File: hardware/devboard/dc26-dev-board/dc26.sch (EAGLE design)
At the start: 105 parts, among them CN1 JST, IC3 LDL112D33R, J1 DC26 Shitty AddOn, J2 DC26 Shitty AddOn, M10 STM32-Breakout-2, P1 SSSS811101, Y1 ABL-8.000MHZ-B2

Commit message: dc26-'final' board ready
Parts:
- removed M10: STM32-Breakout-2, dc-26:M10SILK_FEMALE_PTH
- renumbered CHARGING_CIRCUT to CHARGE
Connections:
- net BUTTON_DOWN: no longer M10.8
- net BUTTON_FIRE1: no longer STM32-BREAKOUT.7
- net BUTTON_LEFT: no longer STM32-BREAKOUT.17
- net BUTTON_RIGHT: no longer STM32-BREAKOUT.5
- net BUTTON_UP: no longer M10.7
- net ESP-IO0: no longer ESP-BREAKOUT.25
- net ESP-RX0: no longer ESP-BREAKOUT.34
- net ESP-TX0: no longer ESP-BREAKOUT.35
- net ESP_I2C_SCL: now also ESP-BREAKOUT.9, STM32-BREAKOUT.5; no longer ESP-BREAKOUT.31, M10.5
- net ESP_I2C_SDA: now also ESP-BREAKOUT.8, STM32-BREAKOUT.3; no longer ESP-BREAKOUT.30, M10.6
- net ESP_INTER: now also STM32-BREAKOUT.8; no longer ESP-BREAKOUT.33, M10.1
- net ESP_RX_PIN_5: no longer ESP-BREAKOUT.29
- net ESP_TX_PIN_4: no longer ESP-BREAKOUT.26
- net GND: now also ESP-BREAKOUT.40; no longer ESP-BREAKOUT.38, M10.9
- net GPIO_APA102_DATA: no longer STM32-BREAKOUT.20
- net GPIO_APA106_DATA: no longer STM32-BREAKOUT.22
- net IO12: now also ESP-BREAKOUT.12; no longer ESP-BREAKOUT.14
- net IO13: now also ESP-BREAKOUT.14; no longer ESP-BREAKOUT.16
- net IO17: now also ESP-BREAKOUT.10; no longer ESP-BREAKOUT.28
- net IO22: now also ESP-BREAKOUT.4; no longer ESP-BREAKOUT.36
- net IO23: now also ESP-BREAKOUT.3; no longer ESP-BREAKOUT.37
- net IO25: now also ESP-BREAKOUT.26; no longer ESP-BREAKOUT.10
- net IO26: now also ESP-BREAKOUT.29; no longer ESP-BREAKOUT.11
- net IO27: now also ESP-BREAKOUT.28; no longer ESP-BREAKOUT.12
- net IO32: now also ESP-BREAKOUT.30; no longer ESP-BREAKOUT.8
- net IO33: now also ESP-BREAKOUT.31; no longer ESP-BREAKOUT.9
- net IO34: now also ESP-BREAKOUT.34; no longer ESP-BREAKOUT.6
- net IO35: now also ESP-BREAKOUT.33; no longer ESP-BREAKOUT.7
- net LCD_BACKLIGHT: no longer STM32-BREAKOUT.34
- net LCD_CS: no longer STM32-BREAKOUT.15
- net LCD_DATA_CMD: no longer STM32-BREAKOUT.13
- net LCD_RESET: no longer STM32-BREAKOUT.40
- net MID_BUTTON: no longer STM32-BREAKOUT.3
- net PA1: now also STM32-BREAKOUT.12; no longer STM32-BREAKOUT.25
- net PA7: now also STM32-BREAKOUT.13; no longer STM32-BREAKOUT.37
- net PB0: now also STM32-BREAKOUT.21; no longer STM32-BREAKOUT.38
- net PB1: now also STM32-BREAKOUT.37; no longer STM32-BREAKOUT.36
- net PB13: now also STM32-BREAKOUT.38; no longer STM32-BREAKOUT.21
- net PB15: now also STM32-BREAKOUT.36; no longer STM32-BREAKOUT.26
- net PB3: now also STM32-BREAKOUT.9; no longer M10.2
- net PB5: now also STM32-BREAKOUT.7; no longer M10.4
- net SENSOR_VN: now also ESP-BREAKOUT.11; no longer ESP-BREAKOUT.5
- net SENSOR_VP: now also ESP-BREAKOUT.16; no longer ESP-BREAKOUT.4
- net SPI2_LCD_MOSI: no longer STM32-BREAKOUT.19
- net SPI2_LCD_SCK: no longer STM32-BREAKOUT.32
- net SPI3_SD_SCK: now also STM32-BREAKOUT.40; no longer STM32-BREAKOUT.30
- net TIM_APA102_CLK: no longer STM32-BREAKOUT.18
- net USART1_RX_TO_ESP_TX_PIN_4: no longer STM32-BREAKOUT.12
- net USART1_TX_TO_ESP_RX_PIN_5: no longer STM32-BREAKOUT.14
- net VCC: no longer M10.10
- net VCC1: now also ESP-BREAKOUT.38
- net VIN: now also ESP-BREAKOUT.39

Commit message: logo causing 0 width polys will fix later
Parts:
- removed U$1: KRUX_LOGO, dc-26:KRUX_LOGO
- removed U$2: CMD_C0DE_LOGO, dc-26:CMD_C0DE_LOGO
- removed U$3: DARKNET_DD, dc-26:DARKNET_DD
- removed U$4: DARKNET_NN, dc-26:DARKNET_NN
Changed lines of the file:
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@@
 <part name="R9" library="dc-26" deviceset="RESISTOR" device="0805-RES" value="1M"/>
 <part name="GND70" library="dc-26" deviceset="GND" device=""/>
-<part name="U$3" library="dc-26" deviceset="DARKNET_D" device="D"/>
-<part name="U$4" library="dc-26" deviceset="DARKNET_N" device="N"/>
 <part name="D1" library="dc-26" deviceset="DIODE" device="SOD" value="1N4148WS"/>
 <part name="102-1" library="dc-26" deviceset="APA102" device="5050"/>
@@
 <part name="J2" library="dc-26" deviceset="DC26_SHITTY_ADDON_CONNECTOR" device="PTH" value="DC26 Shitty AddOn"/>
 <part name="C4" library="dc-26" deviceset="C-US" device="C0805" value="1uF"/>
-<part name="U$1" library="dc-26" deviceset="KRUX_LOGO" device=""/>
-<part name="U$2" library="dc-26" deviceset="CMD_C0DE_LOGO" device=""/>
 </parts>
 <sheets>
@@
 </plain>
 <instances>
-<instance part="U$3" gate="G$1" x="22.86" y="88.9"/>
-<instance part="U$4" gate="G$1" x="30.48" y="88.9"/>
-<instance part="U$1" gate="G$1" x="25.4" y="81.28"/>
-<instance part="U$2" gate="G$1" x="17.78" y="86.36"/>
 </instances>
 <busses>

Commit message: added logo to library added logos to board
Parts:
- added U$1: CMD_C0DE_LOGO, dc-26:CMD_C0DE_LOGO
- added U$2: KRUX_LOGO, dc-26:KRUX_LOGO
- LED1: value MF-LED-0603-GREEN -> MF-LED-1206-GREEN
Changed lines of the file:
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@@
 <part name="GND3" library="dc-26" deviceset="GND" device=""/>
 <part name="GND4" library="dc-26" deviceset="GND" device=""/>
-<part name="LED1" library="dc-26" deviceset="LED" device="1206" value="MF-LED-0603-GREEN"/>
+<part name="LED1" library="dc-26" deviceset="LED" device="1206" value="MF-LED-1206-GREEN"/>
 <part name="LINK1" library="dc-26" deviceset="STLINK-V2-CONNECTOR" device=""/>
 <part name="GND5" library="dc-26" deviceset="GND" device=""/>
@@
 <part name="J2" library="dc-26" deviceset="DC26_SHITTY_ADDON_CONNECTOR" device="PTH" value="DC26 Shitty AddOn"/>
 <part name="C4" library="dc-26" deviceset="C-US" device="C0805" value="1uF"/>
+<part name="U$1" library="dc-26" deviceset="CMD_C0DE_LOGO" device=""/>
+<part name="U$2" library="dc-26" deviceset="KRUX_LOGO" device=""/>
 </parts>
 <sheets>
@@
 </plain>
 <instances>
+<instance part="U$1" gate="G$1" x="45.72" y="91.44"/>
+<instance part="U$2" gate="G$1" x="73.66" y="83.82"/>
 </instances>
 <busses>

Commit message: updated board
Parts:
- RESETTABLE-FUSE: value SSSS811101 -> NANOSMDH075F-02
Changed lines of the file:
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@@
 <part name="LINK1" library="dc-26" deviceset="STLINK-V2-CONNECTOR" device=""/>
 <part name="GND5" library="dc-26" deviceset="GND" device=""/>
-<part name="RESETTABLE-FUSE" library="dc-26" deviceset="PTC" device="SMD" value="SSSS811101"/>
+<part name="RESETTABLE-FUSE" library="dc-26" deviceset="PTC" device="SMD" value="NANOSMDH075F-02"/>
 <part name="P1" library="dc-26" deviceset="SWITCH_SPDT" device="" value="SSSS811101"/>
 <part name="R2" library="dc-26" deviceset="RESISTOR" device="0805-RES" value="470"/>

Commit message: led 3 is now controlled via esp32 rather than STM
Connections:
- net IO14: now also R23.1
- net SIMPLE_LED2: no longer R23.1
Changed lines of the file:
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@@
 <instance part="C39" gate="G$1" x="256.54" y="-96.52"/>
 <instance part="GND64" gate="1" x="241.3" y="-119.38"/>
-<instance part="LED3" gate="G$1" x="151.638" y="149.86"/>
-<instance part="R23" gate="G$1" x="151.638" y="137.16" rot="R90"/>
-<instance part="GND34" gate="1" x="151.638" y="157.48" rot="R180"/>
 <instance part="J1" gate="G$1" x="157.48" y="-30.48"/>
 <instance part="J2" gate="G$1" x="88.9" y="-43.18"/>
@@
 <pinref part="J1" gate="G$1" pin="GND"/>
 <label x="142.24" y="-30.48" size="1.778" layer="95"/>
-</segment>
-<segment>
-<pinref part="LED3" gate="G$1" pin="A"/>
-<pinref part="GND34" gate="1" pin="GND"/>
-<wire x1="151.638" y1="152.4" x2="151.638" y2="154.94" width="0.1524" layer="91"/>
 </segment>
 <segment>
@@
 <wire x1="127" y1="33.02" x2="132.08" y2="33.02" width="0.1524" layer="91"/>
 <label x="132.08" y="33.02" size="1.778" layer="95"/>
-</segment>
-<segment>
-<pinref part="R23" gate="G$1" pin="1"/>
-<wire x1="151.638" y1="132.08" x2="151.638" y2="129.54" width="0.1524" layer="91"/>
-<label x="151.638" y="116.84" size="1.778" layer="95" rot="R90"/>
-</segment>
-</net>
-<net name="N$16" class="0">
-<segment>
-<pinref part="R23" gate="G$1" pin="2"/>
-<pinref part="LED3" gate="G$1" pin="C"/>
-<wire x1="151.638" y1="144.78" x2="151.638" y2="142.24" width="0.1524" layer="91"/>
 </segment>
 </net>
@@
 <instance part="R21" gate="G$1" x="45.72" y="101.6"/>
 <instance part="R22" gate="G$1" x="45.72" y="91.44"/>
+<instance part="LED3" gate="G$1" x="22.098" y="10.16"/>
+<instance part="R23" gate="G$1" x="22.098" y="-2.54" rot="R90"/>
+<instance part="GND34" gate="1" x="22.098" y="17.78" rot="R180"/>
 </instances>
 <busses>
@@
 <wire x1="-40.64" y1="-48.26" x2="-35.56" y2="-48.26" width="0.1524" layer="91"/>
 <label x="-35.56" y="-48.26" size="1.778" layer="95"/>
+</segment>
+<segment>
+<pinref part="LED3" gate="G$1" pin="A"/>
+<pinref part="GND34" gate="1" pin="GND"/>
+<wire x1="22.098" y1="12.7" x2="22.098" y2="15.24" width="0.1524" layer="91"/>
 </segment>
 </net>
@@
 <label x="-50.8" y="45.72" size="1.778" layer="95"/>
 </segment>
+<segment>
+<pinref part="R23" gate="G$1" pin="1"/>
+<wire x1="22.098" y1="-7.62" x2="22.098" y2="-10.16" width="0.1524" layer="91"/>
+<label x="22.098" y="-12.7" size="1.778" layer="95" rot="R90"/>
+</segment>
 </net>
 <net name="SD2" class="0">
@@
 </segment>
 </net>
+<net name="N$16" class="0">
+<segment>
+<pinref part="R23" gate="G$1" pin="2"/>
+<pinref part="LED3" gate="G$1" pin="C"/>
+<wire x1="22.098" y1="5.08" x2="22.098" y2="2.54" width="0.1524" layer="91"/>
+</segment>
+</net>

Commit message: increased the size of the apa106f5 wholes updated ratsnet
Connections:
- removed net SIMPLE_LED2: SOC1.PB14
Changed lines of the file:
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@@
 <wire x1="167.64" y1="50.8" x2="167.64" y2="55.88" width="0.1524" layer="91"/>
 <pinref part="IC3" gate="G$1" pin="EN"/>
+<label x="157.48" y="55.88" size="1.778" layer="95"/>
 </segment>
 </net>
@@
 <wire x1="139.7" y1="137.16" x2="139.7" y2="96.52" width="0.1524" layer="91"/>
 <pinref part="IC3" gate="G$1" pin="VIN"/>
+<label x="116.84" y="78.74" size="1.778" layer="95"/>
 </segment>
 </net>
@@
 </segment>
 </net>
-<net name="SIMPLE_LED2" class="0">
-<segment>
-<pinref part="SOC1" gate="G$1" pin="PB14"/>
-<wire x1="127" y1="33.02" x2="132.08" y2="33.02" width="0.1524" layer="91"/>
-<label x="132.08" y="33.02" size="1.778" layer="95"/>
-</segment>
-</net>
 </nets>
 </sheet>
@@
 <pinref part="C31" gate="G$1" pin="1"/>
 <pinref part="102-1" gate="G$1" pin="VCC"/>
+<label x="12.7" y="99.06" size="1.778" layer="95" rot="R270"/>
 </segment>
 <segment>
@@
 <pinref part="C14" gate="G$1" pin="1"/>
 <pinref part="102-2" gate="G$1" pin="VCC"/>
+<label x="12.7" y="55.88" size="1.778" layer="95" rot="R270"/>
 </segment>
 <segment>
@@
 <pinref part="C20" gate="G$1" pin="1"/>
 <pinref part="102-3" gate="G$1" pin="VCC"/>
+<label x="12.7" y="17.78" size="1.778" layer="95" rot="R270"/>
 </segment>
 <segment>
@@
 <pinref part="C21" gate="G$1" pin="1"/>
 <pinref part="102-4" gate="G$1" pin="VCC"/>
-</segment>
-<segment>
+<label x="12.7" y="-22.86" size="1.778" layer="95" rot="R270"/>
+</segment>
+<segment>

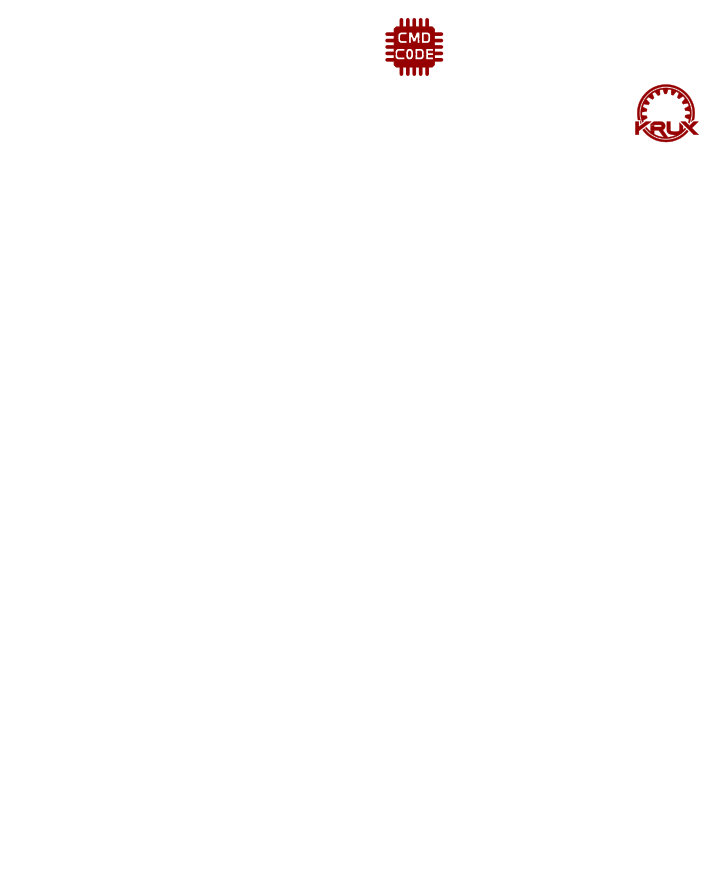
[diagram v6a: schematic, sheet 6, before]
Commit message: Added art work, fixed via drills, and started some initial trace cleanup.  Still need to move Cmdc0de/Krux logos into place.
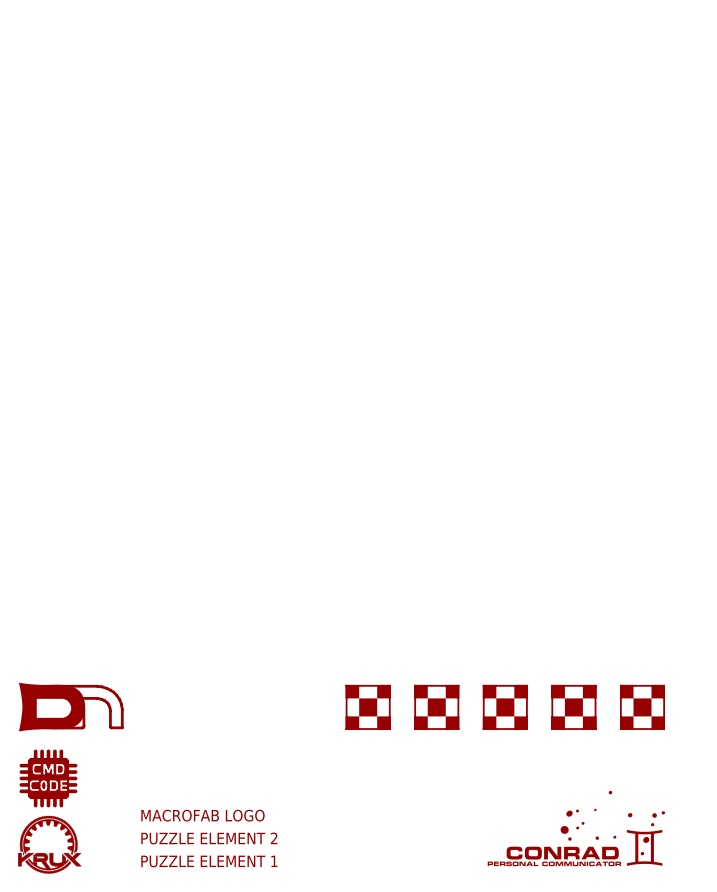
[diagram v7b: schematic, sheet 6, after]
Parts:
- added U$10, U$11, U$9: FIDUCIAL_DNCORNER, darknet_parts_library:FIDUCIAL_DNCORNER
- added U$12: MACROFAB_LOGO, darknet_parts_library:MACROFAB_LOGO
- added U$3: DC26_KRUX_PUZZLE_1, darknet_parts_library:DC26_KRUX_PUZZLE_1
- added U$4: DC26_KRUX_PUZZLE_2, darknet_parts_library:DC26_KRUX_PUZZLE_2
- added U$5: CONRAD_LOGO, darknet_parts_library:CONRAD_LOGO
- added U$6: DN_LOGODC26, darknet_parts_library:DN_LOGODC26
- added U$7, U$8: FIDUCIAL_DNBOX, darknet_parts_library:FIDUCIAL_DNBOX
- U$1: value CMD_C0DE_LOGO -> KRUX_LOGO; device dc-26:CMD_C0DE_LOGO -> darknet_parts_library:KRUX_LOGO
- U$2: value KRUX_LOGO -> CMD_C0DE_LOGO; device dc-26:KRUX_LOGO -> darknet_parts_library:CMD_C0DE_LOGO
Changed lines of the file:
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@@
 <?xml version="1.0" encoding="utf-8"?>
 <!DOCTYPE eagle SYSTEM "eagle.dtd">
-<eagle version="8.7.1">
+<eagle version="7.7.0">
 <drawing>
 <settings>
@@
 <part name="J2" library="dc-26" deviceset="DC26_SHITTY_ADDON_CONNECTOR" device="PTH" value="DC26 Shitty AddOn"/>
 <part name="C4" library="dc-26" deviceset="C-US" device="C0805" value="1uF"/>
-<part name="U$1" library="dc-26" deviceset="CMD_C0DE_LOGO" device=""/>
-<part name="U$2" library="dc-26" deviceset="KRUX_LOGO" device=""/>
+<part name="U$1" library="darknet_parts_library" deviceset="KRUX_LOGO" device=""/>
+<part name="U$2" library="darknet_parts_library" deviceset="CMD_C0DE_LOGO" device=""/>
+<part name="U$3" library="darknet_parts_library" deviceset="DC26_KRUX_PUZZLE_1" device=""/>
+<part name="U$4" library="darknet_parts_library" deviceset="DC26_KRUX_PUZZLE_2" device=""/>
+<part name="U$5" library="darknet_parts_library" deviceset="CONRAD_LOGO" device=""/>
+<part name="U$6" library="darknet_parts_library" deviceset="DN_LOGO" device="DC26"/>
+<part name="U$7" library="darknet_parts_library" deviceset="FIDUCIAL_DN" device="BOX"/>
+<part name="U$8" library="darknet_parts_library" deviceset="FIDUCIAL_DN" device="BOX"/>
+<part name="U$9" library="darknet_parts_library" deviceset="FIDUCIAL_DN" device="CORNER"/>
+<part name="U$10" library="darknet_parts_library" deviceset="FIDUCIAL_DN" device="CORNER"/>
+<part name="U$11" library="darknet_parts_library" deviceset="FIDUCIAL_DN" device="CORNER"/>
+<part name="U$12" library="darknet_parts_library" deviceset="MACROFAB_LOGO" device=""/>
 </parts>
 <sheets>
@@
 <instance part="CHARGE" gate="G$1" x="15.24" y="76.2"/>
 <instance part="GND1" gate="1" x="50.8" y="66.04"/>
-<instance part="GND2" gate="1" x="35.56" y="60.96"/>
+<instance part="GND2" gate="1" x="35.56" y="58.42"/>
 <instance part="GND3" gate="1" x="27.94" y="58.42"/>
 <instance part="GND4" gate="1" x="-22.86" y="68.58"/>
@@
 <pinref part="C1" gate="G$1" pin="2"/>
 <pinref part="GND2" gate="1" pin="GND"/>
+<wire x1="35.56" y1="60.96" x2="35.56" y2="63.5" width="0.1524" layer="91"/>
 </segment>
 <segment>
@@
 </plain>
 <instances>
-<instance part="U$1" gate="G$1" x="45.72" y="91.44"/>
-<instance part="U$2" gate="G$1" x="73.66" y="83.82"/>
+<instance part="U$1" gate="G$1" x="5.08" y="2.54"/>
+<instance part="U$2" gate="G$1" x="5.08" y="10.16"/>
+<instance part="U$3" gate="G$1" x="15.24" y="0"/>
+<instance part="U$4" gate="G$1" x="15.24" y="2.54"/>
+<instance part="U$5" gate="G$1" x="66.04" y="2.54"/>
+<instance part="U$6" gate="G$1" x="12.7" y="15.24"/>
+<instance part="U$7" gate="G$1" x="68.58" y="15.24"/>
+<instance part="U$8" gate="G$1" x="60.96" y="15.24"/>
+<instance part="U$9" gate="G$1" x="53.34" y="15.24"/>
+<instance part="U$10" gate="G$1" x="45.72" y="15.24"/>
+<instance part="U$11" gate="G$1" x="38.1" y="15.24"/>
+<instance part="U$12" gate="G$1" x="15.24" y="5.08"/>
 </instances>
 <busses>
